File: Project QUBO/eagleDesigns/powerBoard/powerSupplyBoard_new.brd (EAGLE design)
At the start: 152.4 x 101.6 mm, 146 parts

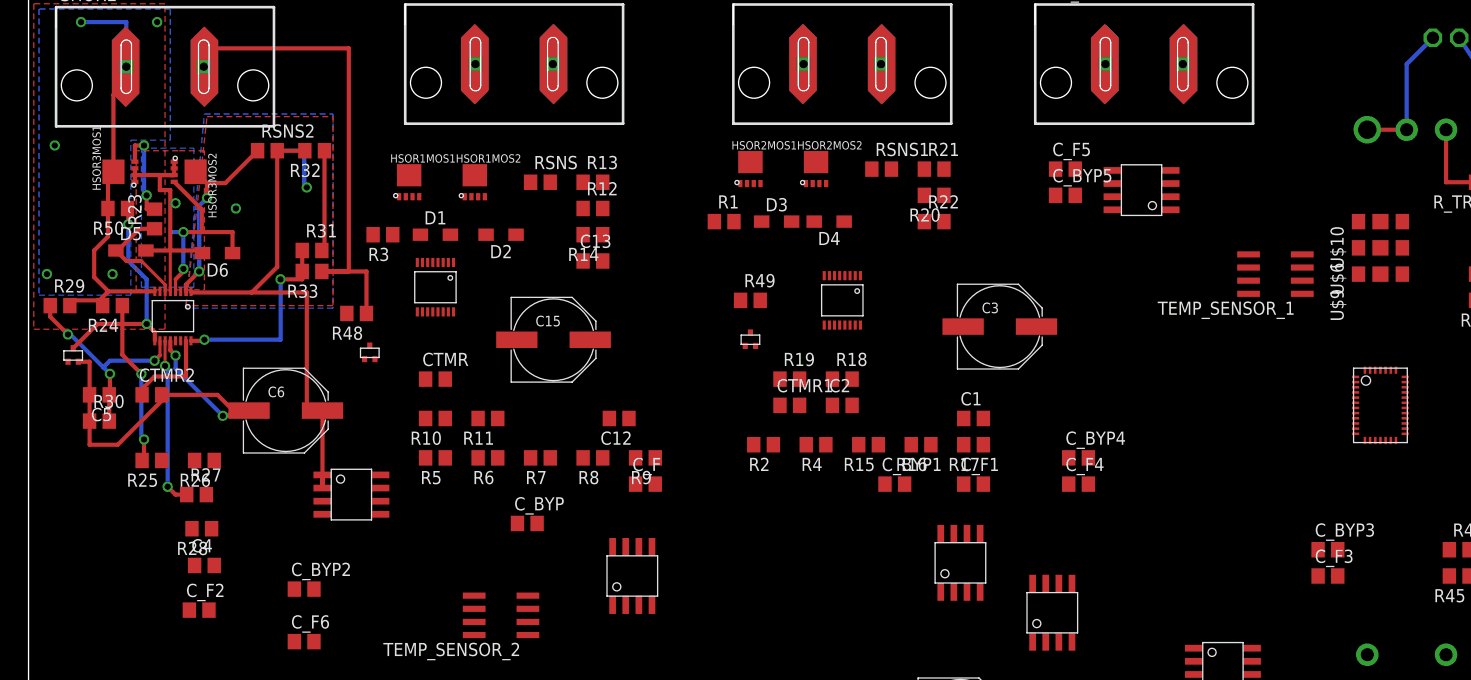
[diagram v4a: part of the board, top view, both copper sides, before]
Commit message: 
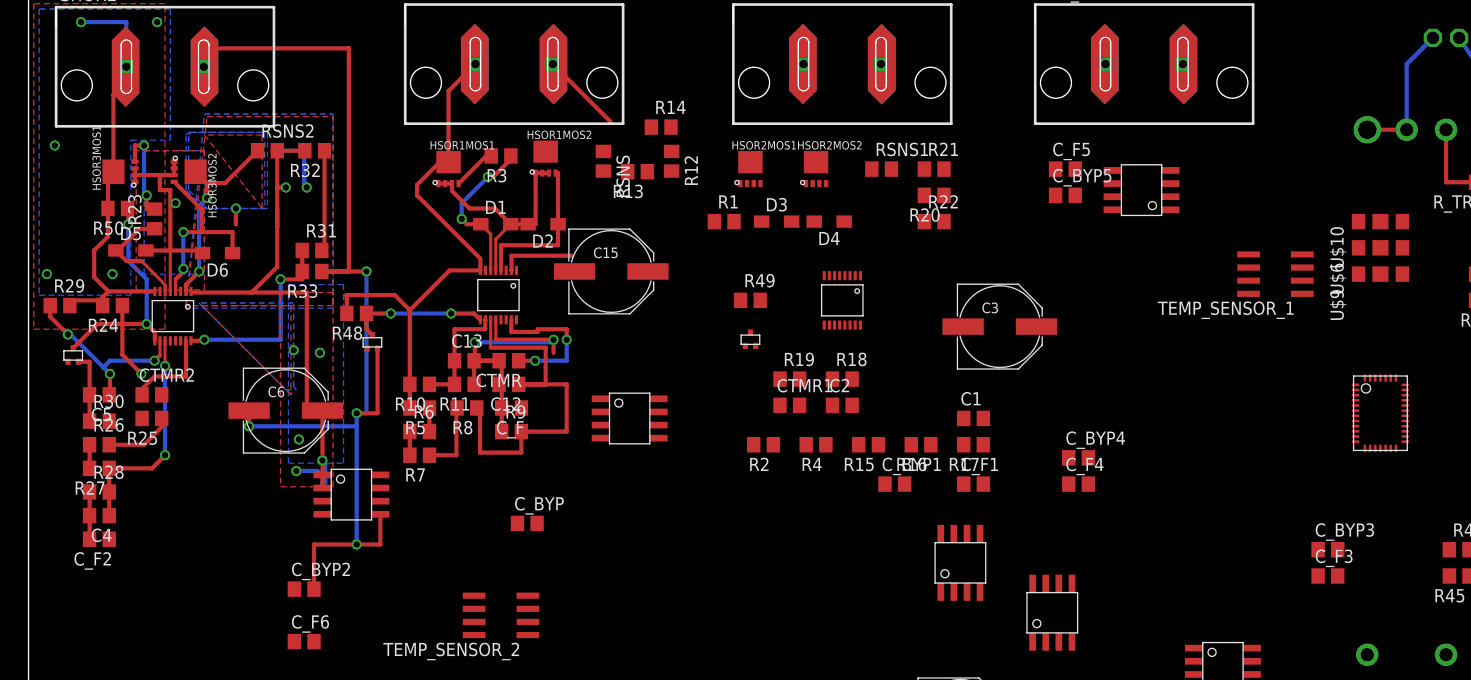
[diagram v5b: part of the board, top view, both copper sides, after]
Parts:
- moved C13 15.8 mm to (42.2, 66.5)
- moved BAT1CS 15.2 mm to (58.2, 61.0), turned to 270 degrees
- moved C_F 14.9 mm to (46.7, 62.0), turned to 180 degrees
- moved R3 13.7 mm to (45.7, 86.4)
- moved R9 13.2 mm to (46.7, 59.7), turned to 0 degrees
- moved R8 13.1 mm to (42.4, 62.0)
- moved R14 12.3 mm to (61.2, 89.2), turned to 0 degrees
- moved C_F2 11.8 mm to (6.86, 49.3), turned to 180 degrees
- moved R7 11.7 mm to (37.8, 57.4)
- moved C4 11.2 mm to (6.86, 51.6), turned to 180 degrees
- moved C12 11.2 mm to (46.5, 64.3)
- moved R28 10.5 mm to (6.86, 53.8), turned to 0 degrees
- moved R26 10.3 mm to (6.86, 58.4), turned to 0 degrees
- moved R27 9.74 mm to (6.86, 56.1), turned to 180 degrees
- moved R12 8.89 mm to (62.2, 85.9), turned to 270 degrees
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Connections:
- new net N$24: BAT1HSOR.SHDN, HIGHSIDEMOS1.D, R48.1
- net GND: no longer BAT1HSOR.SHDN, HIGHSIDEMOS1.D, R48.1
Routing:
- net GND: track 85.4 -> 158.4 mm, vias 2 -> 6
- net BAT1: track 0.00 -> 51.9 mm
- net N$14: track 0.00 -> 38.4 mm
- net N$68: track 0.00 -> 22.8 mm
- net N$7: track 0.00 -> 15.3 mm, vias 0 -> 2
- net N$9: track 0.00 -> 15.2 mm
- net N$20: track 0.00 -> 14.5 mm, vias 0 -> 2
- net N$24: track 0.00 -> 13.6 mm, vias 0 -> 2
- net N$15: track 0.00 -> 11.7 mm
- net BAT3HSOROUT: track 57.2 -> 67.4 mm, vias 2 -> 8
- net N$33: track 15.9 -> 7.37 mm, vias 2 -> 1
- net N$1: track 0.00 -> 7.28 mm
- net N$13: track 0.00 -> 7.24 mm
- net N$34: track 0.00 -> 6.88 mm
- net N$36: track 16.4 -> 21.9 mm
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- added copper zone on layer 1, net N$43
- added copper zone on layer 16, net N$43

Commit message: 
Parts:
- removed ADC: LTC2497UHF, linear:LTC2497-UHF
- removed C_BYP7: .47 uF, resistor:C0805
- removed HIGHSIDEMOS1, HIGHSIDEMOS2, HIGHSIDEMOS3, U$14, U$15: 2SK3019SOT416/SC75, transistor-fet:SOT416
- removed HSOR1MOS1, HSOR1MOS2, HSOR2MOS1, HSOR2MOS2, HSOR3MOS1, HSOR3MOS2: FDMC8360LET40PWR33, fairchild:POWER33
- removed IOEXPANDER: PCF8575C, texas:PW_R-PDSO-G24
- removed JP1: (no value), samtec:MPSC-01-80
- removed R34, R36, R38, R40: 680 kO, resistor:R0805
- removed R35, R37, R39, R41, R43, R44, R45, R47, R48, R49, R50, R51, R52, R53: 100 kO, resistor:R0805
- removed R42: 430 kO, resistor:R0805
- removed R46: 33 kO, resistor:R0805
- removed TEMP_SENSOR_1, TEMP_SENSOR_2: LM35, Jameco:LM35
- removed U$10, U$16, U$17, U$18, U$6, U$9: PULLUP_PULLDOWN0805, resistor:PULLUP_PULLDOWN_0805
- removed U$5: MMSZ5231BSSOD323-REFLOW, diode:SOD323-R
- added U$1, U$2, U$3, U$4, U$7, U$8: FDMC8360LET40, fairchild:FDMC8360LET40
- C15, C3, C6: value 22 uF -> (none)
- D1, D2, D3, D4, D5, D6: device diode:SOD323-W -> diode:SOD523
- moved 16V_CON 596.2 mm to (-96.5, -464.8)
- moved DVL_CON 592.4 mm to (-104.1, -443.2), flipped to the top
- moved R_TRIM 591.0 mm to (-105.4, -453.4), turned to 0 degrees
- moved DVL_12VREG 542.2 mm to (-68.6, -438.1), flipped to the top, turned to 0 degrees
- moved R_LOAD 481.8 mm to (-96.5, -422.9)
- moved C_OUT_5V 477.2 mm to (-92.7, -415.3)
- moved RFBB 469.1 mm to (-96.5, -401.3)
- moved REN_H 464.7 mm to (-96.5, -382.3)
- moved REN_B 462.3 mm to (-96.5, -388.6)
- moved RFBT 459.0 mm to (-96.5, -395.0)
- moved C_IN_5V 458.1 mm to (-96.5, -407.7)
- moved REN_T 455.6 mm to (-96.5, -375.9), turned to 0 degrees
- moved 5VREG 445.9 mm to (-91.4, -358.1), turned to 0 degrees
- moved R_SET3.3V 410.0 mm to (-68.6, -360.7)
- moved C_0_3.3V 406.3 mm to (-77.5, -361.9)
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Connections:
- net BAT1HSOROUT renamed N$39
- net BAT2HSOROUT renamed N$24
- net BAT3HSOROUT renamed N$41
- removed net 12CSOUT: 12VCS.P$7, ADC.CH4
- removed net 12VEN: IOEXPANDER.7, U$14.G
- removed net 16CSOUT: 16VCS.P$7, ADC.CH3
- removed net 3.3CSOUT: 3.3VCS.P$7, ADC.CH6
- removed net 3.3VEN: IOEXPANDER.8, U$15.G
- removed net 5CSOUT: 5VCS.P$7, ADC.CH5
- removed net BAT1CSOUT: ADC.CH0, BAT1CS.P$7
- removed net BAT2CSOUT: ADC.CH1, BAT2CS.P$7
- removed net N$100: JP1.36
- removed net N$24 (its old number): BAT1HSOR.SHDN, HIGHSIDEMOS1.D, R48.1
- removed net N$64: ADC.ADCINN, ADC.MUXOUTP
- removed net N$65: ADC.ADCINP, ADC.MUXOUTN
- removed net N$66: ADC.CH9, R38.1, R39.2
- removed net N$67: ADC.CA2, U$10.MID
- removed net N$68: BAT1HSOR.SOURCE, D1.A, D2.A, HSOR1MOS1.SOURCE1, HSOR1MOS1.SOURCE2, HSOR1MOS1.SOURCE3, HSOR1MOS2.SOURCE1, HSOR1MOS2.SOURCE2, HSOR1MOS2.SOURCE3
- removed net N$69: ADC.CA0, U$6.MID
- removed net N$70: ADC.CA1, U$9.MID
- removed net N$71: ADC.CH10, R40.1, R41.2
- removed net N$72: ADC.CH11, R42.1, R43.2
- removed net N$73: ADC.CH12, R44.1, R45.2
- removed net N$74: ADC.CH13, R46.1, R47.2
- removed net N$83: 3.3VREG.P$6, R_SET3.3V.2
- removed net N$87: 12VREG.P$3, R51.1, U$14.D
- removed net N$88: IOEXPANDER.21, U$17.MID
- removed net N$89: 3.3VREG.P$3, R52.1, U$15.D
- removed net N$90: 12VREG.P$6, R_SET12V.2
- removed net N$92: 5VREG.SS, C_BYP7.1
- removed net N$95: IOEXPANDER.1, R53.1
- removed net N$96: IOEXPANDER.2, U$16.MID
- removed net N$97: IOEXPANDER.3, U$18.MID
- removed net OR1EN: HIGHSIDEMOS1.G, IOEXPANDER.4
- removed net OR2EN: HIGHSIDEMOS2.G, IOEXPANDER.5
- removed net OR3EN: HIGHSIDEMOS3.G, IOEXPANDER.6
- removed net SCL1: ADC.SCL, IOEXPANDER.22, JP1.10
- removed net SDA1: ADC.SDA, IOEXPANDER.23, JP1.9
- removed net SHORECSOUT: ADC.CH2, BAT3CS.P$7
- removed net TEMP1: ADC.CH14, TEMP_SENSOR_1.1
- removed net TEMP2: ADC.CH15, TEMP_SENSOR_2.1
- new net SHORE: SHORE.P$1
- net 12V: no longer JP1.1, JP1.21, JP1.41, JP1.61, R42.2
- net 16V: no longer R40.2
- net 3.3V: no longer JP1.23, JP1.3, JP1.43, JP1.63, R46.2
- net 5V: no longer ADC.REF+, ADC.VCC, IOEXPANDER.24, JP1.2, JP1.22, JP1.42, JP1.62, R44.2, R53.2, TEMP_SENSOR_1.8, TEMP_SENSOR_2.8, U$10.VCC, U$16.VCC, U$17.GND, U$18.VCC, U$6.VCC, U$9.VCC
- net BAT1: now also U$7.DRAIN; no longer HSOR1MOS1.DRAIN, R10.2, R34.2, R48.2
- net BAT2: now also U$1.DRAIN; no longer HSOR2MOS1.DRAIN, R18.2, R36.2, R49.2
- net BAT3: now also U$3.DRAIN; no longer HSOR3MOS1.DRAIN, R29.2, R38.2, R50.2, SHORE.P$1
- net GND: now also 12VREG.P$6, 3.3VREG.P$6, R_SET12V.2, R_SET3.3V.2; no longer 12VREG.P$2, 3.3VREG.P$2, ADC.COM, ADC.F0, ADC.GND0, ADC.GND1, ADC.GND2, ADC.GND3, ADC.GND4, ADC.GND5, ADC.GND6, ADC.REF-, C_0_12V.-, C_0_3.3V.-, C_BYP7.2, HIGHSIDEMOS1.S, HIGHSIDEMOS2.S, HIGHSIDEMOS3.S, IOEXPANDER.12, JP1.12, JP1.15, JP1.18, JP1.24, JP1.33, JP1.34, JP1.37, JP1.39, JP1.4, JP1.40, JP1.44, JP1.64, R35.1, R37.1, R39.1, R41.1, R43.1, R45.1, R47.1, REN_B.1, REN_H.1, REN_T.2, R_SET12V.1, R_SET3.3V.1, TEMP_SENSOR_1.4, TEMP_SENSOR_2.4, U$10.GND, U$14.S, U$15.S, U$16.GND, U$17.VCC, U$18.GND, U$5.A, U$5.C, U$6.GND, U$9.GND
- net N$1: now also BAT1HSOR.SOURCE, D1.A, D2.A, U$7.SOURCE1, U$7.SOURCE2, U$7.SOURCE3, U$8.SOURCE1, U$8.SOURCE2, U$8.SOURCE3; no longer BAT1HSOR.SENSE, HSOR1MOS2.DRAIN, RSNS.1
- net N$11: now also BAT1HSOR.SENSE, RSNS.1, U$8.DRAIN; no longer BAT3HSOR.SOURCE, D5.A, D6.A, HSOR3MOS1.SOURCE1, HSOR3MOS1.SOURCE2, HSOR3MOS1.SOURCE3, HSOR3MOS2.SOURCE1, HSOR3MOS2.SOURCE2, HSOR3MOS2.SOURCE3
- net N$27: now also U$1.SOURCE1, U$1.SOURCE2, U$1.SOURCE3, U$2.SOURCE1, U$2.SOURCE2, U$2.SOURCE3; no longer HSOR2MOS1.SOURCE1, HSOR2MOS1.SOURCE2, HSOR2MOS1.SOURCE3, HSOR2MOS2.SOURCE1, HSOR2MOS2.SOURCE2, HSOR2MOS2.SOURCE3
- net N$28: now also U$1.GATE; no longer HSOR2MOS1.GATE, R1.2
- net N$3: now also U$7.GATE; no longer HSOR1MOS1.GATE, R3.2
- net N$31: now also U$4.GATE; no longer HSOR3MOS2.GATE
- net N$32: now also BAT3HSOR.SENSE, RSNS2.1, U$4.DRAIN; no longer ADC.CH7, R34.1, R35.2
- net N$4: now also U$2.GATE; no longer HSOR2MOS2.GATE
- net N$43: now also BAT3HSOR.SOURCE, D5.A, D6.A, U$3.SOURCE1, U$3.SOURCE2, U$3.SOURCE3, U$4.SOURCE1, U$4.SOURCE2, U$4.SOURCE3; no longer BAT3HSOR.SENSE, HSOR3MOS2.DRAIN, RSNS2.1
- net N$44: now also U$3.GATE; no longer HSOR3MOS1.GATE, R23.2
- net N$5: now also U$2.DRAIN; no longer HSOR2MOS2.DRAIN
- net N$55: now also 12VREG.P$2, C_0_12V.-, R_SET12V.1; no longer ADC.CH8, R36.1, R37.2
- net N$56: now also 3.3VREG.P$2, C_0_3.3V.-, R_SET3.3V.1; no longer BAT3HSOR.SHDN, HIGHSIDEMOS3.D, R50.1
- net N$59: now also REN_B.1, REN_H.1, REN_T.2; no longer BAT2HSOR.SHDN, HIGHSIDEMOS2.D, R49.1
- net N$9: now also U$8.GATE; no longer HSOR1MOS2.GATE
- net VIN: no longer R51.2, R52.2
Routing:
- net GND: track 158.4 -> 0.00 mm, vias 6 -> 0
- net N$41: track 67.4 -> 0.00 mm, vias 8 -> 0
- net BAT1: track 51.9 -> 0.00 mm
- net BAT3: track 42.5 -> 0.00 mm, vias 5 -> 0
- net N$14: track 38.4 -> 0.00 mm
- net N$11: track 25.7 -> 0.00 mm, vias 1 -> 0
- net N$68: track 22.8 -> 0.00 mm
- net N$56: track 22.0 -> 0.00 mm, vias 2 -> 0
- net N$36: track 21.9 -> 0.00 mm, vias 2 -> 0
- net N$40: track 19.5 -> 0.00 mm, vias 2 -> 0
- net N$54: track 19.1 -> 0.00 mm
- net N$43: track 19.1 -> 0.00 mm, vias 2 -> 0
- net N$31: track 18.8 -> 0.00 mm, vias 2 -> 0
- net N$37: track 18.6 -> 0.00 mm, vias 3 -> 0
- net N$7: track 15.3 -> 0.00 mm, vias 2 -> 0
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- removed copper zone on layer 1, net BAT3
- removed copper zone on layer 16, net BAT3
- removed copper zone on layer 1, net N$11
- removed copper zone on layer 16, net N$11
- removed copper zone on layer 1, net N$41
- removed copper zone on layer 16, net N$41
- removed copper zone on layer 1, net N$43
- removed copper zone on layer 16, net N$43
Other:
- board size 152.4 x 101.6 mm -> 100 x 80 mm

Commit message: psb layout updates
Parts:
- removed U$1, U$2, U$3, U$4, U$7, U$8: FDMC8360LET40, fairchild:FDMC8360LET40
- added ADC: LTC2497UHF, linear:LTC2497-UHF
- added C_BYP7: .47 uF, resistor:C0805
- added HIGHSIDEMOS1, HIGHSIDEMOS2, HIGHSIDEMOS3, U$14, U$15: 2SK3019SOT416/SC75, transistor-fet:SOT416
- added HSOR1MOS1, HSOR1MOS2, HSOR2MOS1, HSOR2MOS2, HSOR3MOS1, HSOR3MOS2: FDMC8360LET40PWR33, fairchild:POWER33
- added IOEXPANDER: PCF8575C, texas:PW_R-PDSO-G24
- added JP1: (no value), samtec:MPSC-01-80
- added R34, R36, R38, R40: 680 kO, resistor:R0805
- added R35, R37, R39, R41, R43, R44, R45, R47, R48, R49, R50, R51, R52, R53: 100 kO, resistor:R0805
- added R42: 430 kO, resistor:R0805
- added R46: 33 kO, resistor:R0805
- added TEMP_SENSOR_1, TEMP_SENSOR_2: LM35, Jameco:LM35
- added U$10, U$16, U$17, U$18, U$6, U$9: PULLUP_PULLDOWN0805, resistor:PULLUP_PULLDOWN_0805
- added U$5: MMSZ5231BSSOD323-REFLOW, diode:SOD323-R
- C15, C3, C6: value (none) -> 22 uF
- D1, D2, D3, D4, D5, D6: device diode:SOD523 -> diode:SOD323-W
- moved 16V_CON 596.2 mm to (108.0, 95.2)
- moved DVL_CON 592.4 mm to (137.2, 97.8), flipped to the bottom
- moved R_TRIM 591.0 mm to (141.0, 83.8), turned to 180 degrees
- moved DVL_12VREG 542.2 mm to (137.2, 63.5), flipped to the bottom, turned to 90 degrees
- moved R_LOAD 481.8 mm to (109.2, 12.7)
- moved C_OUT_5V 477.2 mm to (128.3, 7.62)
- moved RFBB 469.1 mm to (114.3, 17.8)
- moved REN_H 464.7 mm to (121.9, 27.9)
- moved REN_B 462.3 mm to (114.3, 22.9)
- moved RFBT 459.0 mm to (114.3, 12.7)
- moved C_IN_5V 458.1 mm to (63.5, 21.6)
- moved REN_T 455.6 mm to (114.3, 27.9), turned to 180 degrees
- moved 5VREG 445.9 mm to (142.2, 21.6), turned to 270 degrees
- moved R_SET3.3V 410.0 mm to (45.7, 33.0)
- moved C_0_3.3V 406.3 mm to (36.8, 27.9)
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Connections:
- net N$24 renamed BAT2HSOROUT
- net N$39 renamed BAT1HSOROUT
- net N$41 renamed BAT3HSOROUT
- removed net SHORE: SHORE.P$1
- new net 12CSOUT: 12VCS.P$7, ADC.CH4
- new net 12VEN: IOEXPANDER.7, U$14.G
- new net 16CSOUT: 16VCS.P$7, ADC.CH3
- new net 3.3CSOUT: 3.3VCS.P$7, ADC.CH6
- new net 3.3VEN: IOEXPANDER.8, U$15.G
- new net 5CSOUT: 5VCS.P$7, ADC.CH5
- new net BAT1CSOUT: ADC.CH0, BAT1CS.P$7
- new net BAT2CSOUT: ADC.CH1, BAT2CS.P$7
- new net N$100: JP1.36
- new net N$24: C13.2, R11.1
- new net N$39: BAT1HSOR.SHDN, HIGHSIDEMOS1.D, R48.1
- new net N$64: ADC.ADCINN, ADC.MUXOUTP
- new net N$65: ADC.ADCINP, ADC.MUXOUTN
- new net N$66: ADC.CH9, R38.1, R39.2
- new net N$67: ADC.CA2, U$10.MID
- new net N$68: BAT1HSOR.SOURCE, D1.A, D2.A, HSOR1MOS1.SOURCE1, HSOR1MOS1.SOURCE2, HSOR1MOS1.SOURCE3, HSOR1MOS2.SOURCE1, HSOR1MOS2.SOURCE2, HSOR1MOS2.SOURCE3
- new net N$69: ADC.CA0, U$6.MID
- new net N$70: ADC.CA1, U$9.MID
- new net N$71: ADC.CH10, R40.1, R41.2
- new net N$72: ADC.CH11, R42.1, R43.2
- new net N$73: ADC.CH12, R44.1, R45.2
- new net N$74: ADC.CH13, R46.1, R47.2
- new net N$83: 3.3VREG.P$6, R_SET3.3V.2
- new net N$87: 12VREG.P$3, R51.1, U$14.D
- new net N$88: IOEXPANDER.21, U$17.MID
- new net N$89: 3.3VREG.P$3, R52.1, U$15.D
- new net N$90: 12VREG.P$6, R_SET12V.2
- new net N$92: 5VREG.SS, C_BYP7.1
- new net N$95: IOEXPANDER.1, R53.1
- new net N$96: IOEXPANDER.2, U$16.MID
- new net N$97: IOEXPANDER.3, U$18.MID
- new net OR1EN: HIGHSIDEMOS1.G, IOEXPANDER.4
- new net OR2EN: HIGHSIDEMOS2.G, IOEXPANDER.5
- new net OR3EN: HIGHSIDEMOS3.G, IOEXPANDER.6
- new net SCL1: ADC.SCL, IOEXPANDER.22, JP1.10
- new net SDA1: ADC.SDA, IOEXPANDER.23, JP1.9
- new net SHORECSOUT: ADC.CH2, BAT3CS.P$7
- new net TEMP1: ADC.CH14, TEMP_SENSOR_1.1
- new net TEMP2: ADC.CH15, TEMP_SENSOR_2.1
- net 12V: now also JP1.1, JP1.21, JP1.41, JP1.61, R42.2
- net 16V: now also R40.2
- net 3.3V: now also JP1.23, JP1.3, JP1.43, JP1.63, R46.2
- net 5V: now also ADC.REF+, ADC.VCC, IOEXPANDER.24, JP1.2, JP1.22, JP1.42, JP1.62, R44.2, R53.2, TEMP_SENSOR_1.8, TEMP_SENSOR_2.8, U$10.VCC, U$16.VCC, U$17.GND, U$18.VCC, U$6.VCC, U$9.VCC
- net BAT1: now also HSOR1MOS1.DRAIN, R10.2, R34.2, R48.2; no longer U$7.DRAIN
- net BAT2: now also HSOR2MOS1.DRAIN, R18.2, R36.2, R49.2; no longer U$1.DRAIN
- net BAT3: now also HSOR3MOS1.DRAIN, R29.2, R38.2, R50.2, SHORE.P$1; no longer U$3.DRAIN
- net GND: now also 12VREG.P$2, 3.3VREG.P$2, ADC.COM, ADC.F0, ADC.GND0, ADC.GND1, ADC.GND2, ADC.GND3, ADC.GND4, ADC.GND5, ADC.GND6, ADC.REF-, C_0_12V.-, C_0_3.3V.-, C_BYP7.2, HIGHSIDEMOS1.S, HIGHSIDEMOS2.S, HIGHSIDEMOS3.S, IOEXPANDER.12, JP1.12, JP1.15, JP1.18, JP1.24, JP1.33, JP1.34, JP1.37, JP1.39, JP1.4, JP1.40, JP1.44, JP1.64, R35.1, R37.1, R39.1, R41.1, R43.1, R45.1, R47.1, REN_B.1, REN_H.1, REN_T.2, R_SET12V.1, R_SET3.3V.1, TEMP_SENSOR_1.4, TEMP_SENSOR_2.4, U$10.GND, U$14.S, U$15.S, U$16.GND, U$17.VCC, U$18.GND, U$5.A, U$5.C, U$6.GND, U$9.GND; no longer 12VREG.P$6, 3.3VREG.P$6, C13.2, R11.1, R_SET12V.2, R_SET3.3V.2
- net N$1: now also BAT1HSOR.SENSE, HSOR1MOS2.DRAIN, RSNS.1; no longer BAT1HSOR.SOURCE, D1.A, D2.A, U$7.SOURCE1, U$7.SOURCE2, U$7.SOURCE3, U$8.SOURCE1, U$8.SOURCE2, U$8.SOURCE3
- net N$11: now also BAT3HSOR.SOURCE, D5.A, D6.A, HSOR3MOS1.SOURCE1, HSOR3MOS1.SOURCE2, HSOR3MOS1.SOURCE3, HSOR3MOS2.SOURCE1, HSOR3MOS2.SOURCE2, HSOR3MOS2.SOURCE3; no longer BAT1HSOR.SENSE, RSNS.1, U$8.DRAIN
- net N$27: now also HSOR2MOS1.SOURCE1, HSOR2MOS1.SOURCE2, HSOR2MOS1.SOURCE3, HSOR2MOS2.SOURCE1, HSOR2MOS2.SOURCE2, HSOR2MOS2.SOURCE3; no longer U$1.SOURCE1, U$1.SOURCE2, U$1.SOURCE3, U$2.SOURCE1, U$2.SOURCE2, U$2.SOURCE3
- net N$28: now also HSOR2MOS1.GATE, R1.2; no longer U$1.GATE
- net N$3: now also HSOR1MOS1.GATE, R3.2; no longer U$7.GATE
- net N$31: now also HSOR3MOS2.GATE; no longer U$4.GATE
- net N$32: now also ADC.CH7, R34.1, R35.2; no longer BAT3HSOR.SENSE, RSNS2.1, U$4.DRAIN
- net N$4: now also HSOR2MOS2.GATE; no longer U$2.GATE
- net N$43: now also BAT3HSOR.SENSE, HSOR3MOS2.DRAIN, RSNS2.1; no longer BAT3HSOR.SOURCE, D5.A, D6.A, U$3.SOURCE1, U$3.SOURCE2, U$3.SOURCE3, U$4.SOURCE1, U$4.SOURCE2, U$4.SOURCE3
- net N$44: now also HSOR3MOS1.GATE, R23.2; no longer U$3.GATE
- net N$5: now also HSOR2MOS2.DRAIN; no longer U$2.DRAIN
- net N$55: now also ADC.CH8, R36.1, R37.2; no longer 12VREG.P$2, C_0_12V.-, R_SET12V.1
- net N$56: now also BAT3HSOR.SHDN, HIGHSIDEMOS3.D, R50.1; no longer 3.3VREG.P$2, C_0_3.3V.-, R_SET3.3V.1
- net N$59: now also BAT2HSOR.SHDN, HIGHSIDEMOS2.D, R49.1; no longer REN_B.1, REN_H.1, REN_T.2
- net N$9: now also HSOR1MOS2.GATE; no longer U$8.GATE
- net VIN: now also R51.2, R52.2
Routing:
- net GND: track 0.00 -> 159.1 mm, vias 0 -> 7
- net BAT3HSOROUT: track 0.00 -> 55.7 mm, vias 0 -> 4
- net N$1: track 0.00 -> 42.7 mm, vias 0 -> 5
- net BAT3: track 0.00 -> 42.5 mm, vias 0 -> 5
- net BAT1HSOROUT: track 0.00 -> 34.2 mm, vias 0 -> 2
- net N$15: track 0.00 -> 33.2 mm, vias 0 -> 3
- net BAT1: track 0.00 -> 33.2 mm, vias 0 -> 5
- net N$17: track 0.00 -> 28.6 mm
- net N$68: track 0.00 -> 27.9 mm, vias 0 -> 2
- net N$8: track 0.00 -> 26.5 mm, vias 0 -> 2
- net N$11: track 0.00 -> 25.7 mm, vias 0 -> 1
- net N$45: track 0.00 -> 24.3 mm
- net N$14: track 0.00 -> 23.3 mm
- net N$56: track 0.00 -> 22.0 mm, vias 0 -> 2
- net N$37: track 0.00 -> 21.1 mm, vias 0 -> 3
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- added copper zone on layer 1, net BAT1
- added copper zone on layer 16, net BAT1
- added copper zone on layer 1, net BAT1HSOROUT
- added copper zone on layer 1, net BAT3
- added copper zone on layer 16, net BAT3
- added copper zone on layer 1, net BAT3HSOROUT
- added copper zone on layer 16, net BAT3HSOROUT
- added copper zone on layer 16, net N$1
- added copper zone on layer 1, net N$11
- added copper zone on layer 16, net N$11
- added copper zone on layer 1, net N$43
- added copper zone on layer 16, net N$43
- added copper zone on layer 1, net N$68
- added copper zone on layer 16, net N$68
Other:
- board size 100 x 80 mm -> 152.4 x 101.6 mm
